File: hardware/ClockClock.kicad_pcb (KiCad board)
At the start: 2 copper layers, 50.8 x 39.4 mm, 13 parts, among them J1 OLED, J2 PWR_EN, J3 BUZZ_CON, J4 VIBE_CON, J5 LED_CON, Q1 irfz44l, Q2 irfz44l, Q3 irfz44l, U1 3a_dcdc_vreg_board, U2 WeMos_mini

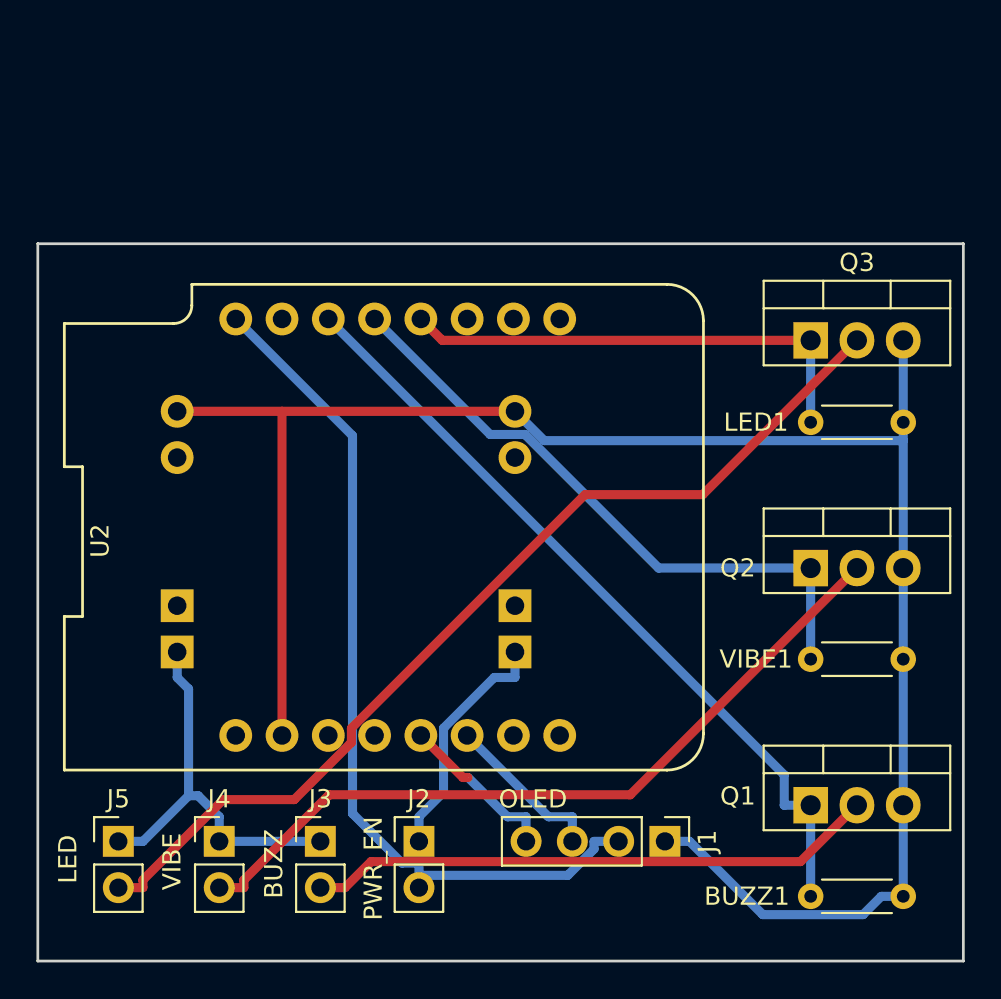
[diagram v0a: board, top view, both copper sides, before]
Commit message: directory clean up and better more finalized layout
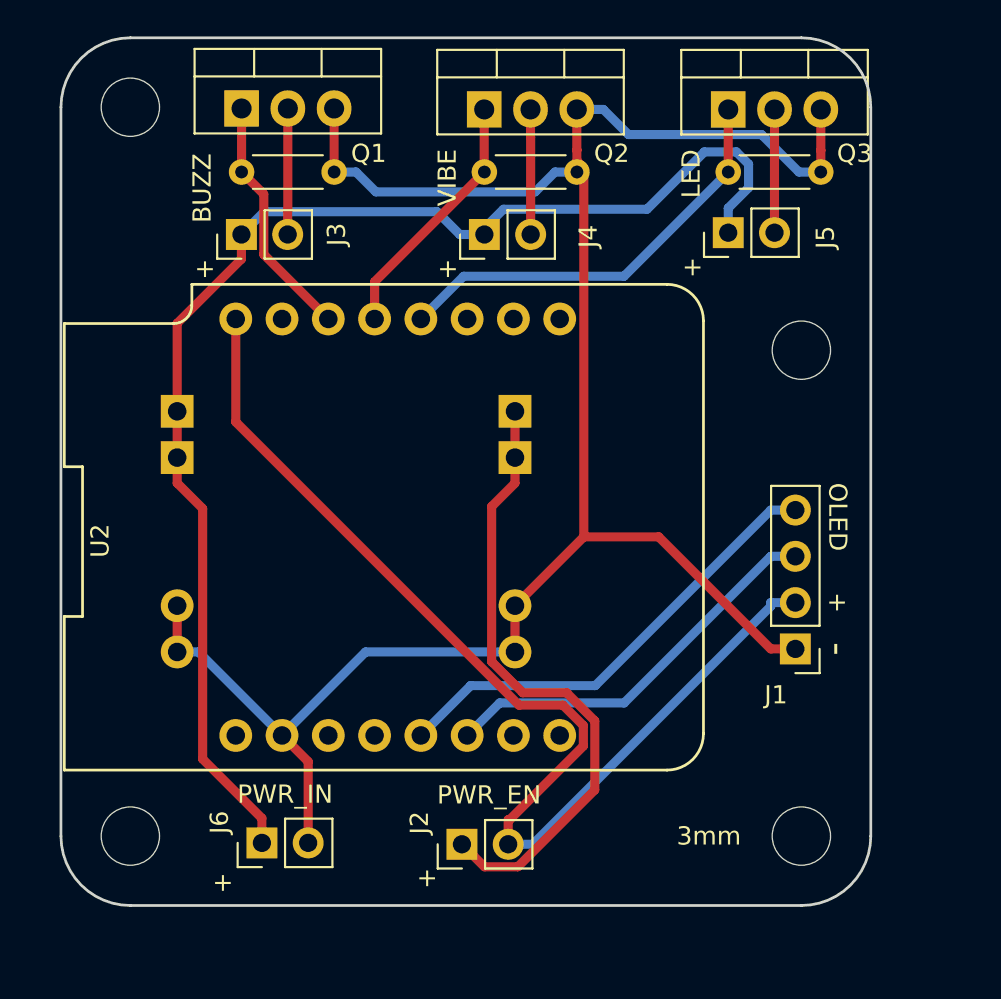
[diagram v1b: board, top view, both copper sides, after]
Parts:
- added J6: +12V_IN, Connector_PinHeader_2.54mm:PinHeader_1x02_P2.54mm_Vertical, F.Cu at (80.9, 156.6)
- added m1: MountingHole_3.2mm_M3, MountingHole:MountingHole_3.2mm_M3, F.Cu at (73.7, 116.2)
- added m2: MountingHole_3.2mm_M3, MountingHole:MountingHole_3.2mm_M3, F.Cu at (110.5, 129.5)
- added m3: MountingHole_3.2mm_M3, MountingHole:MountingHole_3.2mm_M3, F.Cu at (73.7, 156.2)
- added m4: MountingHole_3.2mm_M3, MountingHole:MountingHole_3.2mm_M3, F.Cu at (110.5, 156.2)
- Q1, Q2, Q3: value irfz44l -> IRLZ44N
- moved BUZZ 50.6 mm to (79.8, 119.8)
- moved Q1 49.4 mm to (79.8, 116.3)
- moved J5 47.3 mm to (106.5, 123.1), turned to 90 degrees
- moved J4 36.3 mm to (93.1, 123.2), turned to 90 degrees
- moved J3 33.6 mm to (79.8, 123.2), turned to 90 degrees
- moved VIBE 32.2 mm to (93.1, 119.8)
- moved Q2 30.9 mm to (93.1, 116.3)
- moved LED 14.5 mm to (106.5, 119.8)
- moved Q3 13.5 mm to (106.5, 116.3)
- moved J1 12.8 mm to (110.2, 145.9), turned to 180 degrees
- moved J2 2.36 mm to (91.9, 156.7), turned to 90 degrees
- renumbered BUZZ1 to BUZZ, LED1 to LED, VIBE1 to VIBE
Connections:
- U1 pad 1: +12V -> GND
- U1 pad 2: Net-(U1-Pad2) -> GND
- U1 pad 3: Net-(U1-Pad3) -> GND
- U1 pad 5: Net-(J2-Pad1) -> +12V
- U1 pad 6: Net-(U1-Pad6) -> Net-(J2-Pad1)
- U1 pad 7: Net-(U1-Pad7) -> +12V
- U1 pad 8: GND -> Net-(J2-Pad1)
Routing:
- net +12V: track 22.1 -> 72.4 mm
- net Net-(J5-Pad2): track 53.7 -> 6.76 mm
- net Net-(J4-Pad2): track 42.5 -> 6.87 mm
- net Net-(BUZZ1-Pad1): track 43.5 -> 13.5 mm
- net Net-(J3-Pad2): track 31.3 -> 6.92 mm
- net Net-(J2-Pad1): track 13.2 -> 34.6 mm
- net Net-(Q2-Pad1): track 34.6 -> 14.0 mm
- net Net-(J1-Pad4): track 8.97 -> 25.7 mm, vias 1 -> 0
- net Net-(J1-Pad2): track 47.9 -> 61.3 mm
- net Net-(J1-Pad3): track 8.97 -> 22.1 mm
- net GND: track 104.0 -> 113.6 mm
- net Net-(LED1-Pad1): track 26.4 -> 23.6 mm
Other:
- board size 50.8 x 39.4 mm -> 44.5 x 47.6 mm
- net class Default: clearance 0.05 -> 0.127
- rule trace_clearance: 0.05 -> 0.127
- rule trace_min: 0.006 -> 0.127
- rule via_min_drill: 0.013 -> 0.2
- rule via_min_size: 0.027 -> 0.45
- board text added: "+"
- board text added: "-"
- board text added: "3mm"
- board text added: "PWR_IN"
- board text removed: "BUZZ"
- board text removed: "LED"
- board text removed: "VIBE"

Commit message: Finalized board layout and added some pictures to the info
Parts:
- added J7: OFF_BTN, Connector_PinHeader_2.54mm:PinHeader_1x02_P2.54mm_Vertical, F.Cu at (98.0, 156.6)
- moved J2 2.54 mm to (89.3, 156.7)
- renumbered BUZZ to BUZZ1, LED to LED1, VIBE to VIBE1
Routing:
- net GND: track 113.6 -> 130.3 mm
- net Net-(J2-Pad1): track 34.6 -> 49.3 mm
- net Net-(J7-Pad1): track 0.00 -> 13.4 mm
- net +12V: track 72.4 -> 66.8 mm
- net Net-(J1-Pad3): track 22.1 -> 25.8 mm
- net Net-(J1-Pad4): track 25.7 -> 28.4 mm
- net Net-(J1-Pad2): track 61.3 -> 63.3 mm
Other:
- net class Power added: clearance 0.127, trace_width 1.5, via_dia 0.45, via_drill 0.2
- board text added: "ClockClock V1"
- board text added: "OFF_BTN"
